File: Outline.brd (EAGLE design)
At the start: 53.8 x 53.8 mm, 44 parts, among them CN1 0675031020, IC1 ATXMEGA32A4U-AU, IC2 ST1480ACDR, J1 RJHSE5080, Q1 BC817-16, U1 NCP1117DTAG @ 3.3v, U2 NCP1117DTAG @ 12v, X1 0470531000

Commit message: Version 3
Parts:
- removed U$1: LABEL_JUMPER_1X3, dp_devices:JUMP3_DESC
- removed X1: 0470531000, con-molex:KK-156-4
- added J2: J2, TechIsCool:47053-1000
- added PDI: AVR_PDI, TechIsCool:AVR_PDI
- added R13: 4.7k Ohm, nonolith:0603
- added R14: 11.8k, nonolith:0603
- added R15: 10k, nonolith:0603
- C1, C14, C6, C7: device nonolith:0805 -> SparkFun:0603-CAP
- CN1: device adafruit:USB-MINIB -> TechIsCool:MOLEX_675031020
- J1: device con-amp:520426-4 -> TechIsCool:RJHSE5080
- JP1: value (none) -> JUMPER_3; device jumper:JP2 -> TechIsCool:JP2E
- R1, R8: value 300 mOhm -> 300m Ohm
- U$2: value AVR_PDI -> DS18B20; device TechIsCool:AVR_PDI -> TechIsCool:TOP-92-INLINE
- moved IC2 30.6 mm to (23.4, 47.0), turned to 0 degrees
- moved CN1 27.8 mm to (48.6, 33.2), turned to 0 degrees
- moved U$2 17.8 mm to (17.9, 40.2), flipped to the bottom, turned to 315 degrees
- moved R11 13.3 mm to (50.5, 43.4), turned to 0 degrees
- moved R10 11.7 mm to (50.5, 41.9), turned to 0 degrees
- moved J1 9.02 mm to (19.3, -1.02)
- moved C7 8.32 mm to (47.1, 40.5), turned to 0 degrees
- moved C6 7.74 mm to (37.2, 35.0), turned to 315 degrees
- moved R12 7.31 mm to (46.3, 51.0), turned to 90 degrees
- moved C1 6.10 mm to (30.8, 47.5), turned to 225 degrees
- moved IC1 4.93 mm to (38.7, 44.0), turned to 315 degrees
- moved R6 4.15 mm to (39.5, 17.6), turned to 180 degrees
- moved JP1 3.82 mm to (13.7, 35.1)
- moved C5 1.30 mm to (11.4, 42.2)
- moved C14 1.01 mm to (43.5, 50.5), turned to 135 degrees
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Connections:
- removed net N$16: CN1.D+, IC1.27
- removed net N$17: IC2.7, J1.5
- removed net N$18: IC2.6, J1.6
- removed net N$19: CN1.D-, IC1.26
- removed net N$23: IC1.32, IC2.1
- removed net N$24: IC1.33, IC2.3
- new net ONE_WIRE_TEMP: IC1.14, R13.1, U$2.2
- new net RS485_N: IC2.7, J1.P$1
- new net RS485_P: IC2.6, J1.P$2
- new net RX: IC1.12, IC2.1
- new net TX: IC1.13, IC2.4
- new net USB+: CN1.P$3, IC1.27
- new net USB-: CN1.P$2, IC1.26
- new net VBUS_SENSE: IC1.25, R14.2, R15.1
- net +12V: now also J2.3; no longer X1.3
- net +15V: now also J1.P$7, J1.P$8; no longer J1.1, J1.2
- net +3V3: now also PDI.2, R13.2, U$2.3; no longer U$2.2
- net +5V: now also CN1.P$1, R14.1; no longer CN1.VBUS
- net FAN_PWM: now also J2.1; no longer X1.1
- net FAN_RPM: now also IC1.33; no longer IC1.14
- net GND: now also CN1.GND@1, CN1.GND@2, CN1.GND@3, CN1.GND@4, CN1.P$5, J1.P$5, J1.P$6, J2.4, PDI.6, R15.2, U$2.1; no longer CN1.GND, J1.7, J1.8, U$2.6, X1.4
- net N$20: now also PDI.1; no longer U$2.1
- net N$22: now also PDI.5; no longer U$2.5
- net N$25: now also J2.2; no longer X1.2
- net RX_EN: now also IC1.1; no longer IC1.28
- net TX_EN: now also IC1.2, IC2.3; no longer IC1.29, IC2.4
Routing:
- net RS485_N: track 0.00 -> 72.9 mm, vias 0 -> 1
- net RS485_P: track 0.00 -> 72.4 mm, vias 0 -> 1
- net N$17: track 44.5 -> 0.00 mm, vias 1 -> 0
- net N$18: track 41.5 -> 0.00 mm, vias 1 -> 0
- net N$16: track 27.9 -> 0.00 mm, vias 2 -> 0
- net N$19: track 26.8 -> 0.00 mm, vias 2 -> 0
- net +5V: track 13.6 -> 39.2 mm, vias 0 -> 1
- net N$23: track 23.8 -> 0.00 mm, vias 2 -> 0
- net N$20: track 25.7 -> 7.00 mm, vias 1 -> 0
- net N$24: track 17.4 -> 0.00 mm, vias 2 -> 0
- net ONE_WIRE_TEMP: track 0.00 -> 16.4 mm
- net +3V3: track 115.8 -> 99.4 mm, vias 1 -> 3
- net FAN_SWITCH: track 21.0 -> 36.6 mm
- net N$22: track 20.5 -> 8.02 mm, vias 2 -> 1
- net RX: track 0.00 -> 12.4 mm
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- added copper zone on layer 1, net +3V3
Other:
- outline, holes or cut-outs redrawn
- board text added: "15v"
- board text added: "5v"
- board text added: "Copyright 2012 TechIsCool v1.0"
- board text added: "High Brightness RGB LED Driver"
- board text added: "http://TechIsCool.com"

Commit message: Version 4
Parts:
- added C11, C13, C15, C9: .1uF, SparkFun:0603-CAP
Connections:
- net +12V: now also C15.1
- net +15V: now also C13.1
- net +3V3: now also C9.1
- net GND: now also C11.2, C13.2, C15.2, C9.2
- net N$21: now also C11.1
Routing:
- net +3V3: track 99.4 -> 96.4 mm, vias 3 -> 8
- net N$21: track 24.8 -> 27.3 mm
- net +12V: track 33.4 -> 35.7 mm, vias 0 -> 5
- net FAN_SWITCH: track 36.6 -> 35.2 mm
- added copper zone on layer 16, net +12V
- added copper zone on layer 16, net +3V3

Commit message: Version 4.1
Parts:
- removed Q1: BC817-16, dp_devices:SOT-23
- removed R7: 1k Ohm, nonolith:0603
- added U$1: DMG1012T, TechIsCool:DMG1012T
- R2: value 102k Ohm -> 15 Ohms
- R3: value 62k Ohm -> 9.09 Ohms
- R4: value 102k Ohm -> 102 Ohms
- R5: value 11.8k Ohm -> 11.8 Ohms
- moved R6 17.2 mm to (50.0, 4.06), turned to 90 degrees
- moved R10 1.55 mm to (50.8, 40.4)
- moved R11 0.92 mm to (50.8, 42.5)
- moved C7 0.38 mm to (47.4, 40.5)
- moved J2 0.25 mm to (39.1, 6.60)
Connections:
- new net N$4: R6.2, U$1.P$G
- net +12V: now also JP1.3
- net +15V: no longer JP1.3
- net FAN_SWITCH: now also R6.1; no longer R6.2
- net GND: now also U$1.P$S; no longer J2.4, Q1.2, R7.2
- net N$2: no longer Q1.3
- net N$3: now also J2.4, U$1.P$D; no longer Q1.1, R6.1, R7.1
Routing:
- net +12V: track 35.7 -> 85.3 mm, vias 5 -> 6
- net FAN_SWITCH: track 35.2 -> 65.1 mm
- net +15V: track 180.2 -> 171.6 mm
- net N$25: track 41.9 -> 49.2 mm
- net GND: track 7.39 -> 12.8 mm, vias 13 -> 15
- net N$4: track 0.00 -> 2.77 mm
- net N$2: track 8.29 -> 5.89 mm
- net N$3: track 4.54 -> 3.11 mm
- net +3V3: track 96.4 -> 97.3 mm
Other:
- board text added: "12v"
- board text removed: "15v"

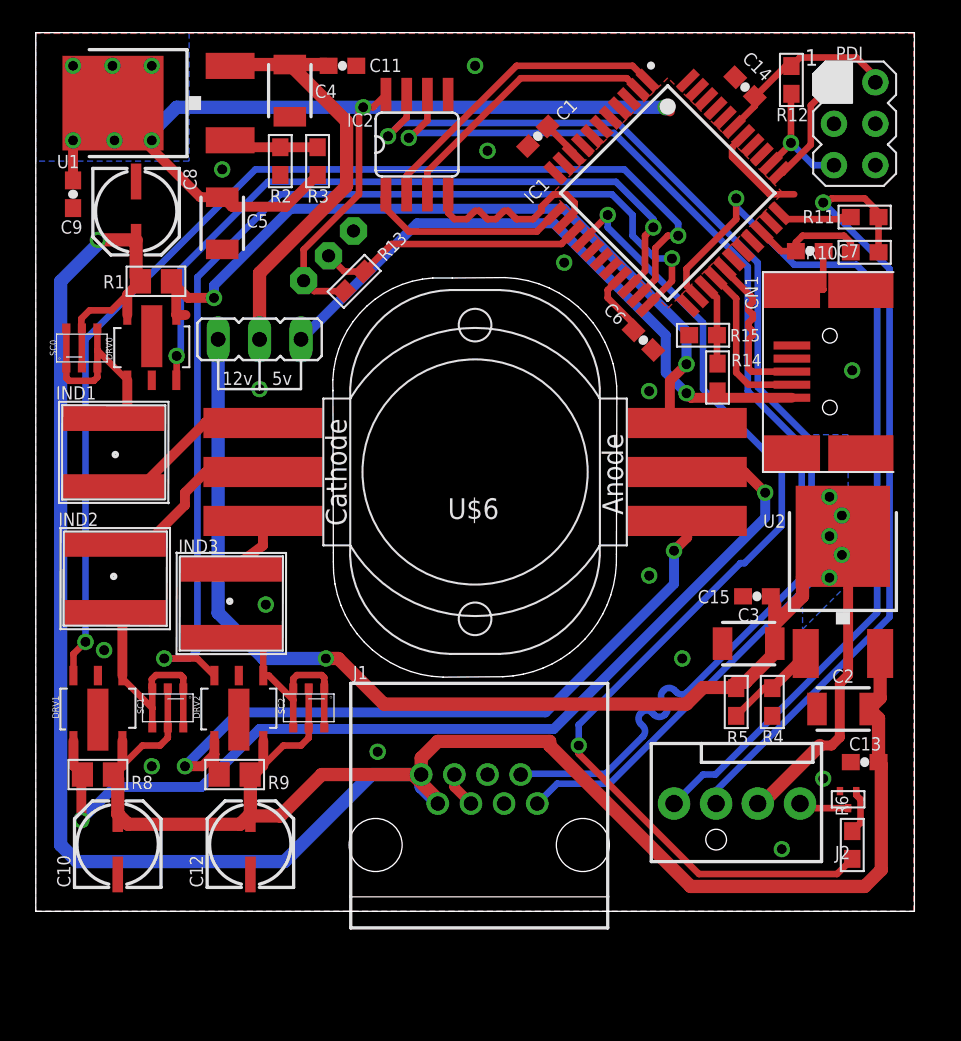
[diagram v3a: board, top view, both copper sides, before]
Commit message: Cleaned Up some
Still have a trace broken though
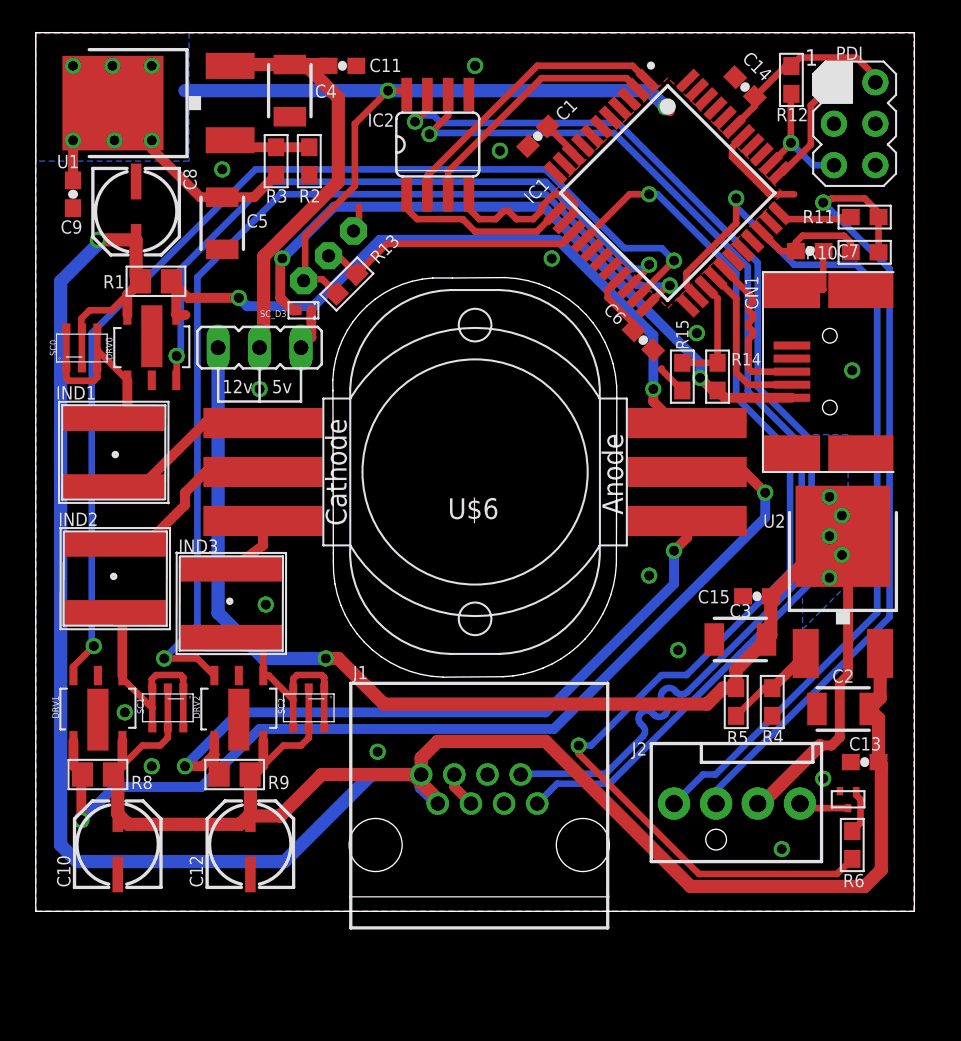
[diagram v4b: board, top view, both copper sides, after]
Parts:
- added SC_D3: 1PS74SB23, TechIsCool:NSR05F20
- moved R15 2.84 mm to (39.6, 32.8), turned to 270 degrees
- moved R3 2.54 mm to (14.7, 46.0)
- moved R2 1.78 mm to (16.8, 46.0)
- moved IC2 1.27 mm to (24.6, 47.0)
- moved C3 0.57 mm to (43.2, 16.7)
- moved JP1 0.51 mm to (13.7, 34.5)
- moved R13 0.48 mm to (19.1, 38.4)
- moved R14 0.05 mm to (41.8, 32.8)
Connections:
- new net N$6: JP1.1, SC_D3.P$1
- net +5V: now also SC_D3.P$2; no longer JP1.1
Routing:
- net +3V3: track 97.3 -> 86.0 mm
- net FAN_SWITCH: track 65.1 -> 70.3 mm
- net RED_A: track 47.3 -> 43.3 mm
- net GND: track 12.8 -> 16.3 mm
- net +5V: track 39.2 -> 42.2 mm, vias 1 -> 2
- net RS485_N: track 72.9 -> 70.3 mm
- net N$6: track 0.00 -> 2.55 mm
- net VBUS_SENSE: track 4.97 -> 7.12 mm
- net PWM2: track 65.7 -> 63.5 mm
- net PWM1: track 68.8 -> 66.8 mm
- net TX: track 12.3 -> 10.5 mm
- net PWM0: track 43.8 -> 42.0 mm
- net RS485_P: track 72.4 -> 70.7 mm
- net RX: track 12.4 -> 11.0 mm
- net TX_EN: track 17.0 -> 15.7 mm
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
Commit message: Still have an airwire
Not sure why
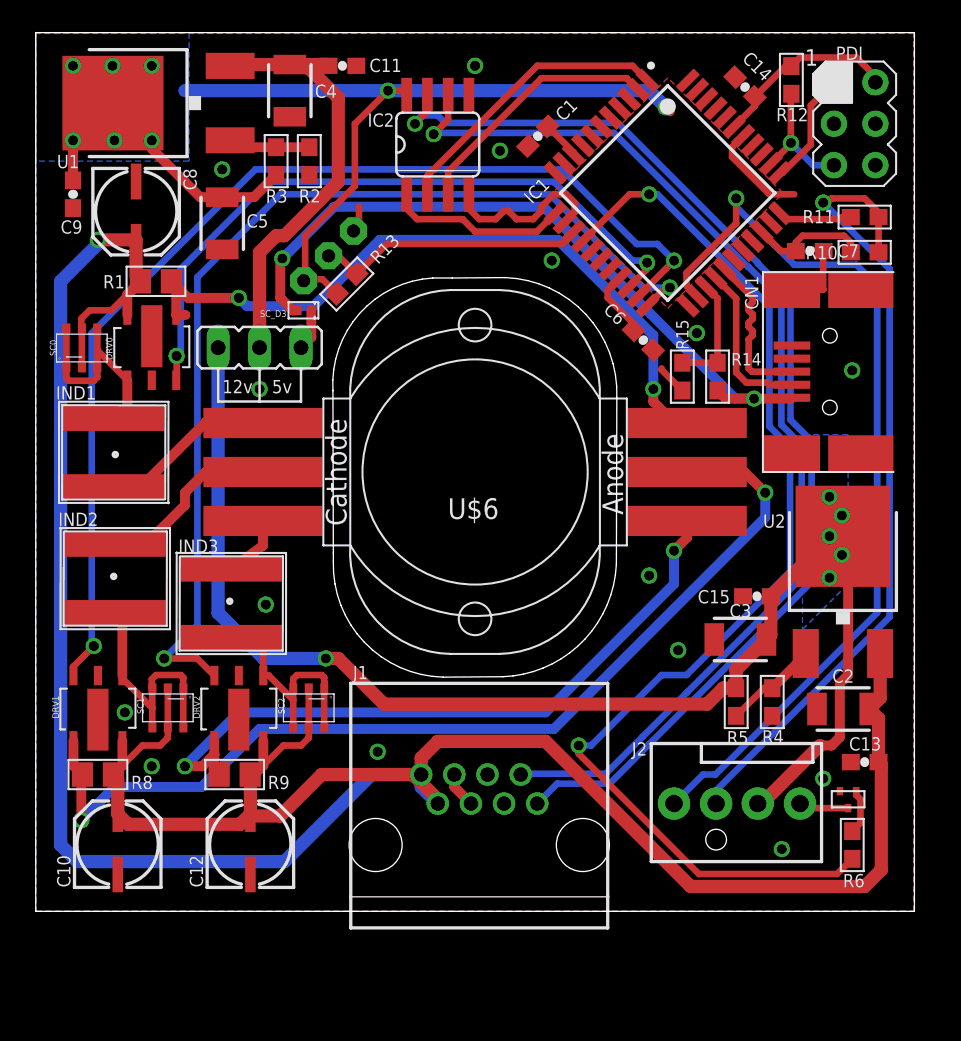
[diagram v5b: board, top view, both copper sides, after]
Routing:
- net RS485_P: track 70.7 -> 68.4 mm
- net +3V3: track 86.0 -> 88.3 mm
- net +5V: track 42.2 -> 43.9 mm
- net +12V: track 84.2 -> 85.4 mm
- net PWM2: track 63.5 -> 63.0 mm
